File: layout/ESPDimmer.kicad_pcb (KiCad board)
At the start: 2 copper layers, 36 x 31 mm, 11 parts, among them P1 CONN_01X03, P2 Serial, P3 LED, P4 ProgMod, Q1 IRLB8721, U1 TLV1117, U2 ESP-12E

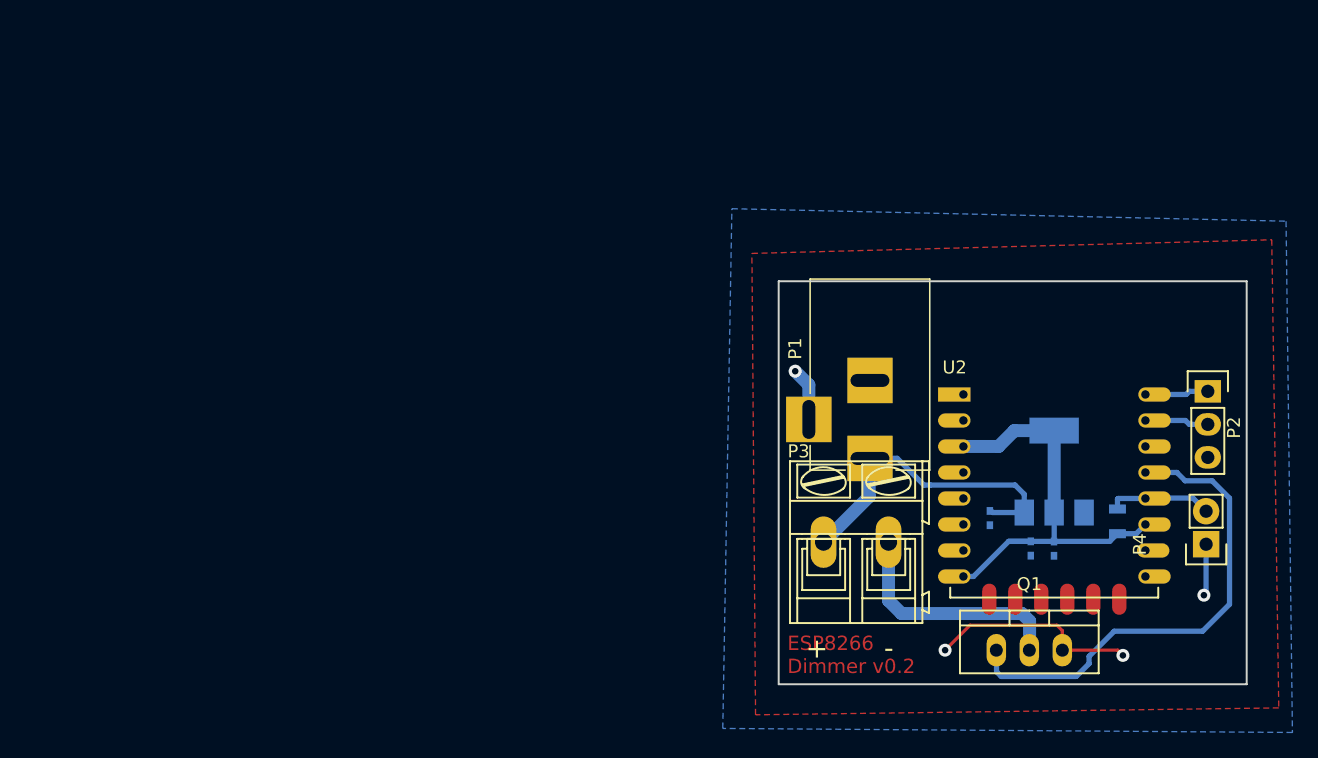
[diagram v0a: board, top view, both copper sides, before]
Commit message: Updated schematic and PCB, initial firmware (no wifi, only encoder control)
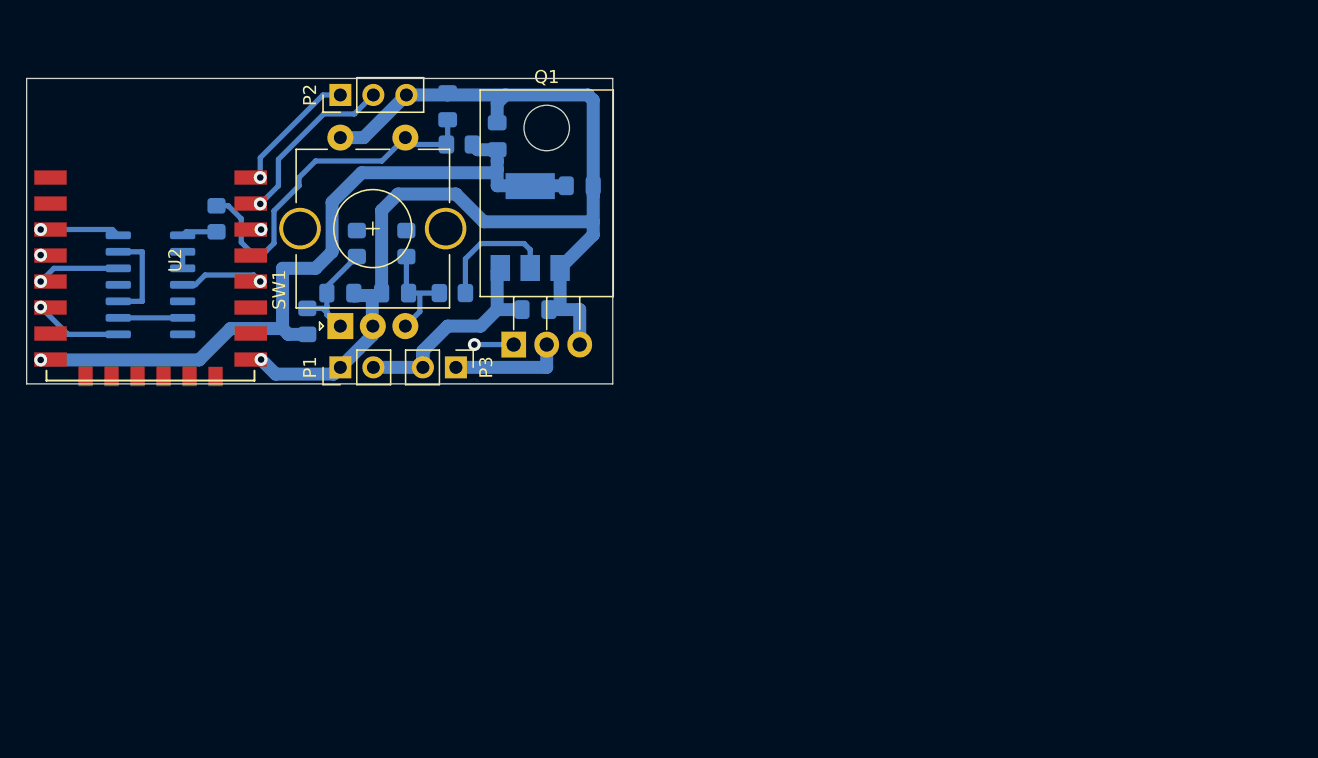
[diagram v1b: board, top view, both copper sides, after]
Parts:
- removed P4: ProgMod, Socket_Strips:Socket_Strip_Straight_1x02
- added C4: 100n, Capacitor_SMD:C_0805_2012Metric_Pad1.18x1.45mm_HandSolder, B.Cu at (87.6, 80.0)
- added C5: 100n, Capacitor_SMD:C_0805_2012Metric_Pad1.18x1.45mm_HandSolder, B.Cu at (95.9, 65.6)
- added C6: 100n, Capacitor_SMD:C_0805_2012Metric_Pad1.18x1.45mm_HandSolder, B.Cu at (91.8, 80.0)
- added R2: 10k, Resistor_SMD:R_0805_2012Metric_Pad1.20x1.40mm_HandSolder, B.Cu at (96.8, 68.6)
- added R3: 10k, Resistor_SMD:R_0805_2012Metric_Pad1.20x1.40mm_HandSolder, B.Cu at (96.2, 80.0)
- added R4: 1k, Resistor_SMD:R_0805_2012Metric_Pad1.20x1.40mm_HandSolder, B.Cu at (88.9, 76.2)
- added R5: 1k, Resistor_SMD:R_0805_2012Metric_Pad1.20x1.40mm_HandSolder, B.Cu at (78.1, 74.3)
- added R6: 1k, Resistor_SMD:R_0805_2012Metric_Pad1.20x1.40mm_HandSolder, B.Cu at (92.7, 76.2)
- added SW1: Rotary_Encoder_Switch, Rotary_Encoder:RotaryEncoder_Alps_EC11E-Switch_Vertical_H20mm_CircularMountingHoles, F.Cu at (87.6, 82.5)
- added U3: 74HC14, Package_SO:SOIC-14_3.9x8.7mm_P1.27mm, B.Cu at (73.0, 79.4)
- C1, C2, C3: footprint Capacitors_SMD:C_0402 -> Capacitor_SMD:C_0805_2012Metric_Pad1.18x1.45mm_HandSolder
- P1: value CONN_01X03 -> IN; footprint Connect:BARREL_JACK -> Connector_PinHeader_2.54mm:PinHeader_1x02_P2.54mm_Vertical
- P2: footprint Socket_Strips:Socket_Strip_Straight_1x03 -> Connector_PinHeader_2.54mm:PinHeader_1x03_P2.54mm_Vertical
- P3: value LED -> OUT; footprint Connect:AK300-2 -> Connector_PinHeader_2.54mm:PinHeader_1x02_P2.54mm_Vertical
- Q1: value IRLB8721 -> IRLZ44N; footprint TO_SOT_Packages_THT:TO-220_Neutral123_Vertical -> Package_TO_SOT_THT:TO-220-3_Horizontal_TabDown
- R1: footprint Resistors_SMD:R_0805 -> Resistor_SMD:R_0805_2012Metric_Pad1.20x1.40mm_HandSolder
- U1: value TLV1117 -> AMS1117-3.3; footprint TO_SOT_Packages_SMD:SOT-223 -> Package_TO_SOT_SMD:SOT-223-3_TabPin2
- U2: footprint ESP8266:ESP-12E -> ESP8266:ESP-12E_SMD_CHI
- moved U2 71.5 mm to (66.0, 71.1)
- moved P2 70.5 mm to (87.6, 64.8), turned to 90 degrees
- moved R1 64.2 mm to (85.1, 82.2)
- moved C2 53.3 mm to (99.7, 67.9), turned to 90 degrees
- moved Q1 46.1 mm to (101.0, 84.0)
- moved C3 44.5 mm to (106.0, 71.8), turned to 0 degrees
- moved U1 44.5 mm to (102.2, 74.9)
- moved P1 41.3 mm to (87.6, 85.7), turned to 90 degrees
- moved C1 38.5 mm to (102.6, 81.3), turned to 0 degrees
- moved P3 31.3 mm to (96.5, 85.7), turned to 270 degrees
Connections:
- P1 pad 1: VCC -> GND
- P1 pad 2: GND -> VCC
- P2 pad 1: /TX -> Net-(P2-Pad1)
- P2 pad 2: /RX -> Net-(P2-Pad2)
- P3 pad 1: VCC -> /-V
- P3 pad 2: /-V -> VCC
- R1 pad 2: /GPIO0 -> Net-(C4-Pad1)
- U2 pad 10: GND -> Net-(U2-Pad10)
- U2 pad 11: +3V3 -> Net-(U2-Pad11)
- U2 pad 12: /GPIO0 -> Net-(U2-Pad12)
- U2 pad 13: Net-(Q1-Pad1) -> Net-(U2-Pad13)
- U2 pad 15: /RX -> GND
- U2 pad 16: /TX -> Net-(U2-Pad16)
- U2 pad 20: Net-(U2-Pad20) -> Net-(Q1-Pad1)
- U2 pad 21: Net-(U2-Pad21) -> Net-(P2-Pad2)
- U2 pad 22: Net-(U2-Pad22) -> Net-(P2-Pad1)
- U2 pad 4: Net-(U2-Pad4) -> GND
- U2 pad 9: GND -> Net-(U2-Pad9)
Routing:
- net GND: track 24.5 -> 86.8 mm, vias 4 -> 2
- net +3V3: track 33.4 -> 74.1 mm, vias 0 -> 2
- net Net-(Q1-Pad1): track 37.8 -> 3.03 mm, vias 0 -> 2
- net Net-(C5-Pad1): track 0.00 -> 28.0 mm
- net Net-(P2-Pad2): track 0.00 -> 13.4 mm, vias 0 -> 1
- net /-V: track 19.2 -> 8.74 mm
- net Net-(C4-Pad1): track 0.00 -> 10.1 mm
- net Net-(P2-Pad1): track 0.00 -> 9.68 mm, vias 0 -> 1
- net Net-(C6-Pad1): track 0.00 -> 8.06 mm
- net /GPIO0: track 8.03 -> 0.00 mm
- net Net-(U3-Pad10): track 0.00 -> 7.49 mm
- net Net-(U2-Pad6): track 0.00 -> 6.93 mm, vias 0 -> 1
- net VCC: track 25.1 -> 18.5 mm
- net Net-(U2-Pad18): track 0.00 -> 6.49 mm, vias 0 -> 1
- net Net-(U2-Pad5): track 0.00 -> 6.39 mm, vias 0 -> 1
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- removed copper zone on B.Cu, net GND
- removed copper zone on F.Cu, net GND
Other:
- board size 36 x 31 mm -> 45.1 x 23.5 mm
- board text removed: "+"
- board text removed: "-"
- board text removed: "ESP8266 Dimmer v0.2"

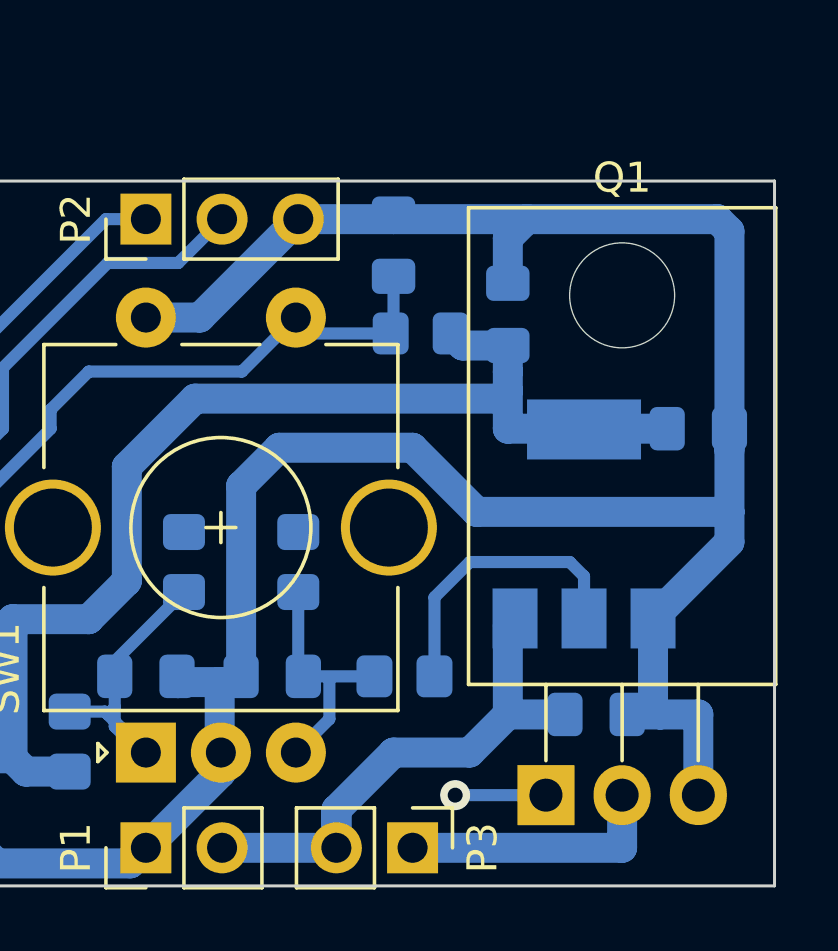
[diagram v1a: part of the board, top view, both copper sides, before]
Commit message: Added NTP and basic web UI
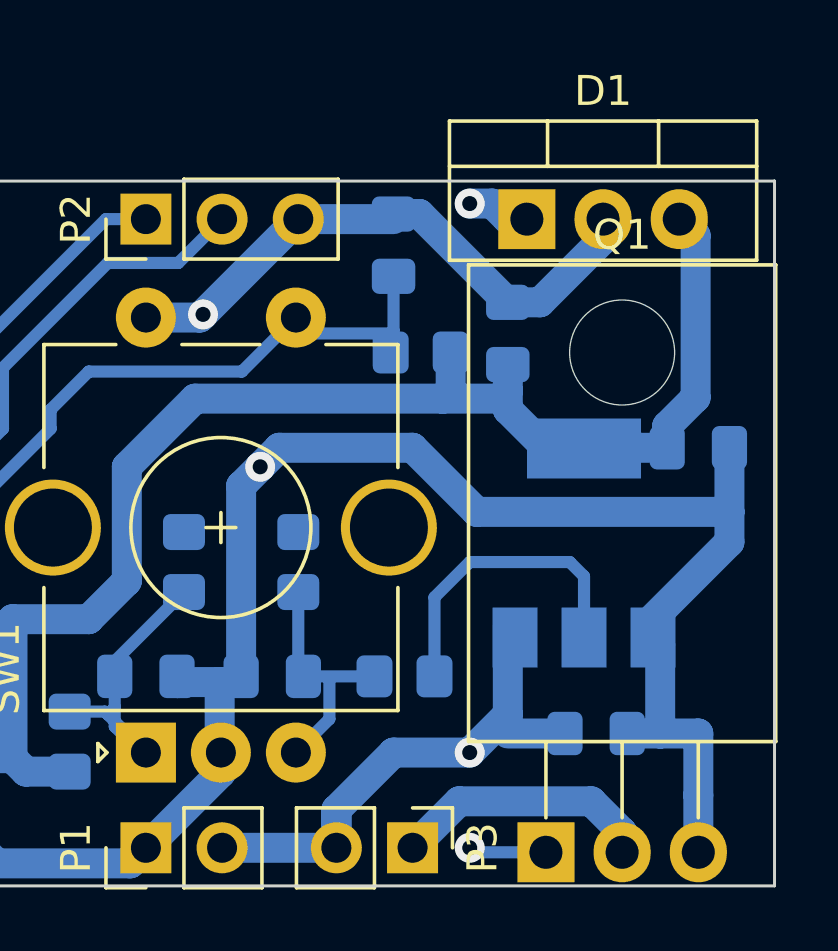
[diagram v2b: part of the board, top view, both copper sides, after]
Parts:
- added D1: StepDown3V3, Package_TO_SOT_THT:TO-220-3_Vertical, F.Cu at (100.3, 64.8)
- moved Q1 1.91 mm to (101.0, 85.9)
- moved C1 0.64 mm to (102.6, 81.9)
- moved C2 0.64 mm to (99.7, 68.6)
- moved C3 0.64 mm to (106.0, 72.4)
- moved R2 0.64 mm to (96.8, 69.2)
- moved U1 0.63 mm to (102.2, 75.6)
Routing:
- net GND: track 86.8 -> 76.1 mm, vias 2 -> 4
- net +3V3: track 74.1 -> 80.9 mm
- net VCC: track 18.5 -> 20.3 mm, vias 0 -> 2
